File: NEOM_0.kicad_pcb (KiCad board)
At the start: 2 copper layers, 28 x 24 mm, 21 parts, among them U1 LM3940, U2 7_Pins_Header_PA0_PA6, U3 Reset Button, U4 STM32F070F6P6, U6 7_Pins_Header_PA7_PA14, U7 TPD4S012DRYR, U8 16Mhz, U9 USB_Micro_B

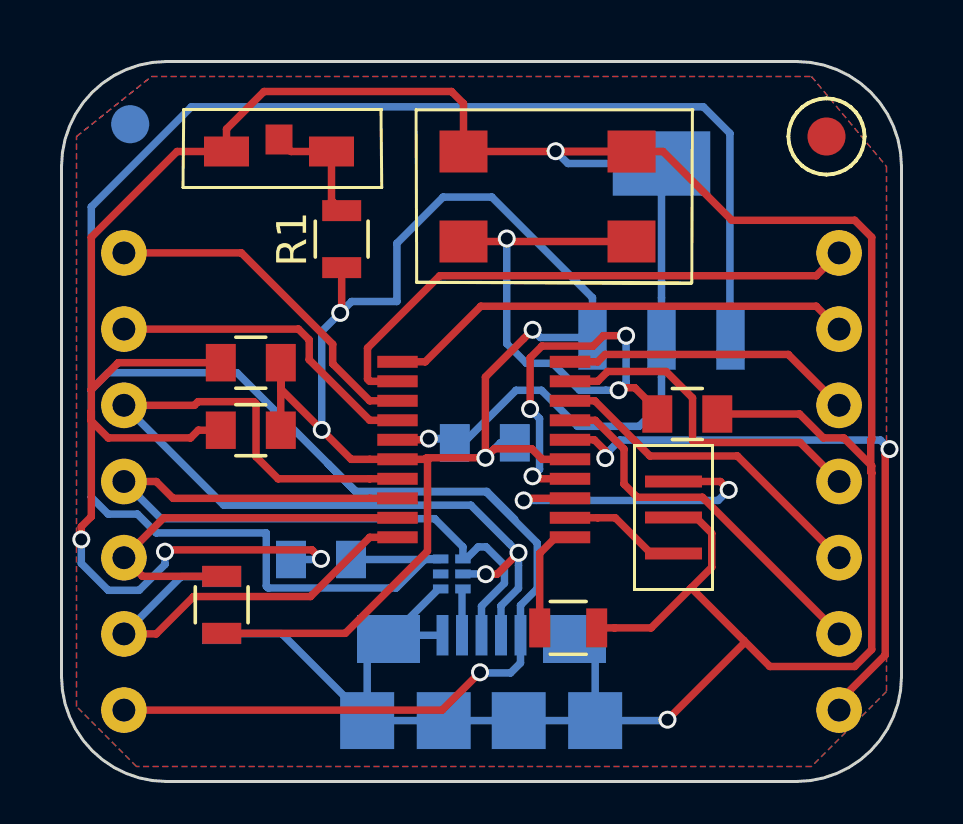
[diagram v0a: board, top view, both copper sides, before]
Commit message: Updated PCB with Footprint Fab..
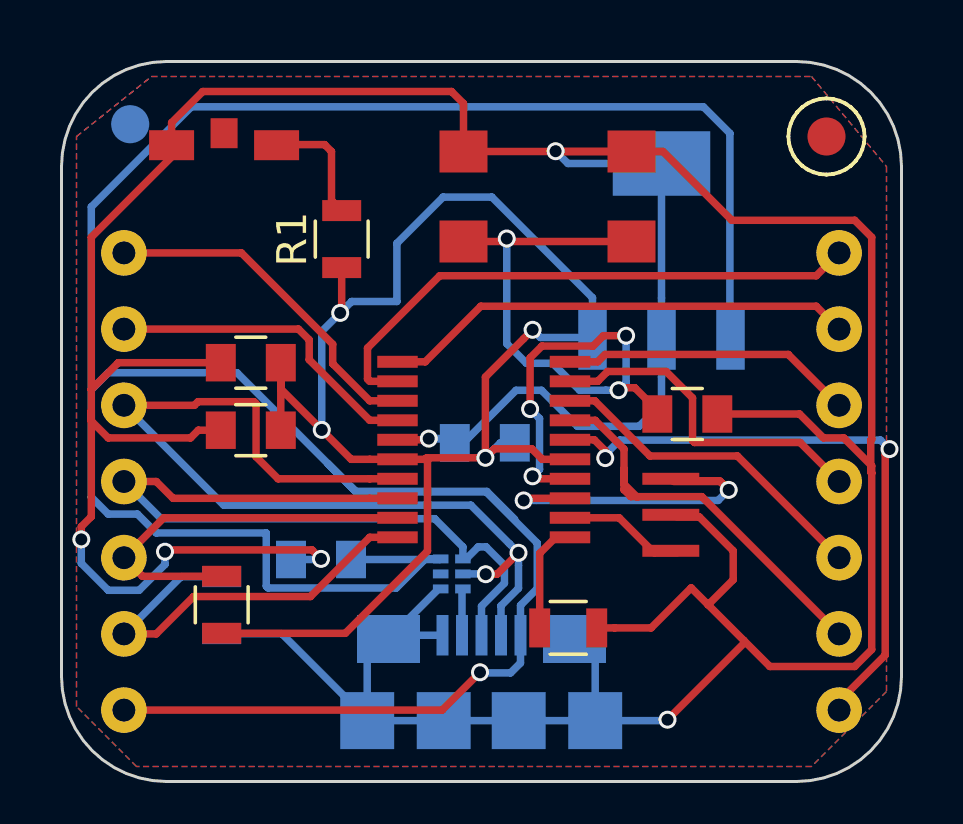
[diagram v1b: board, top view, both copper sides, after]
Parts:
- C1, C2, C3, C4, C5: footprint Capacitors_SMD:C_0805 -> Footprints2:C_0805
- D1: footprint Footprints:0805_LED -> Footprints2:0805_LED
- U1: footprint Footprints:LM3940 -> Footprints2:LM3940
- U3: footprint Footprints:Tactile_Button -> Footprints2:Tactile_Button
- U4: footprint Footprints:TSSOP20 -> Footprints2:TSSOP20
- U7: footprint Footprints:TPD4S012DRYR -> Footprints2:TPD4S012DRYR
- U8: footprint Footprints:16Mhz -> Footprints2:16Mhz
- moved D1 4.60 mm to (115.5, 92.1)
- moved U8 2.91 mm to (130.3, 104.1)
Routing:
- net Net-(U4-Pad3): track 10.5 -> 12.4 mm
- net Net-(U2-Pad2): track 12.6 -> 13.8 mm
- net GND: track 152.5 -> 153.5 mm

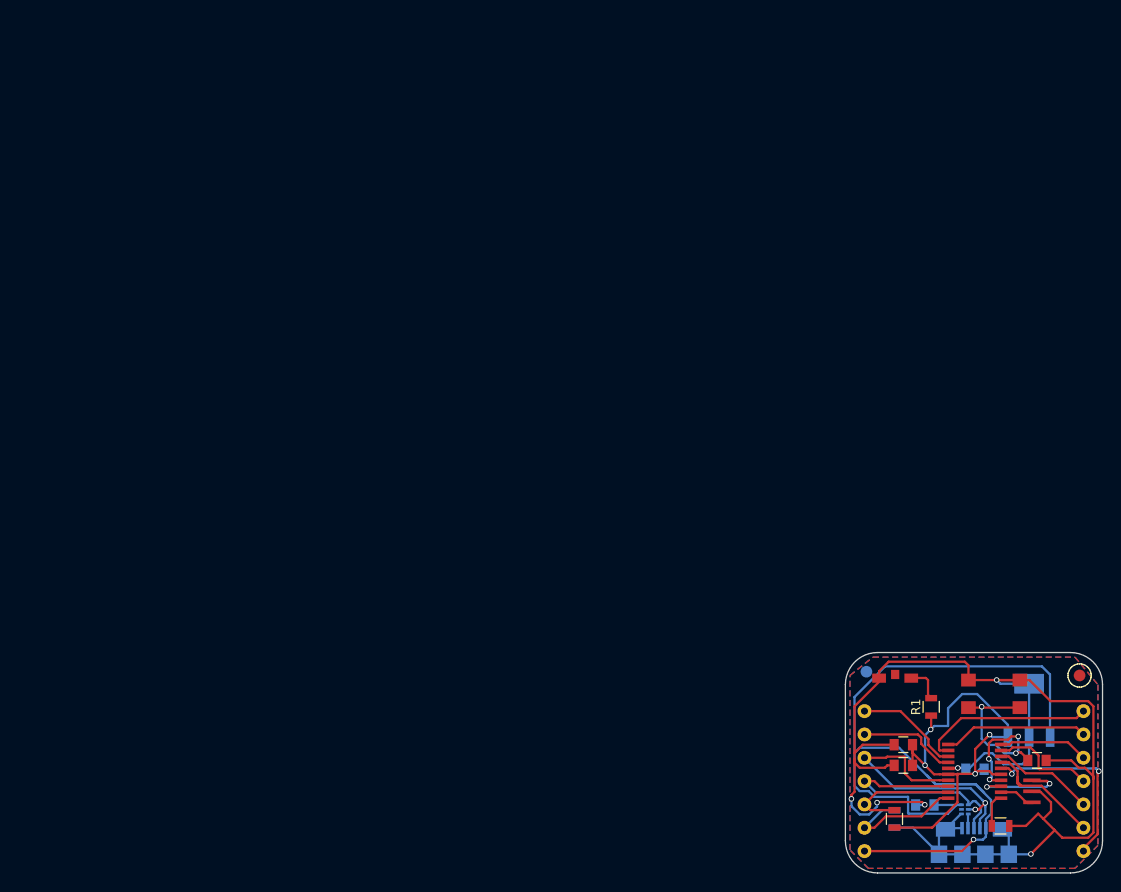
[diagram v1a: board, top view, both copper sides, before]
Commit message: Updated PCB: added defferintial pair routing to USB+/-...
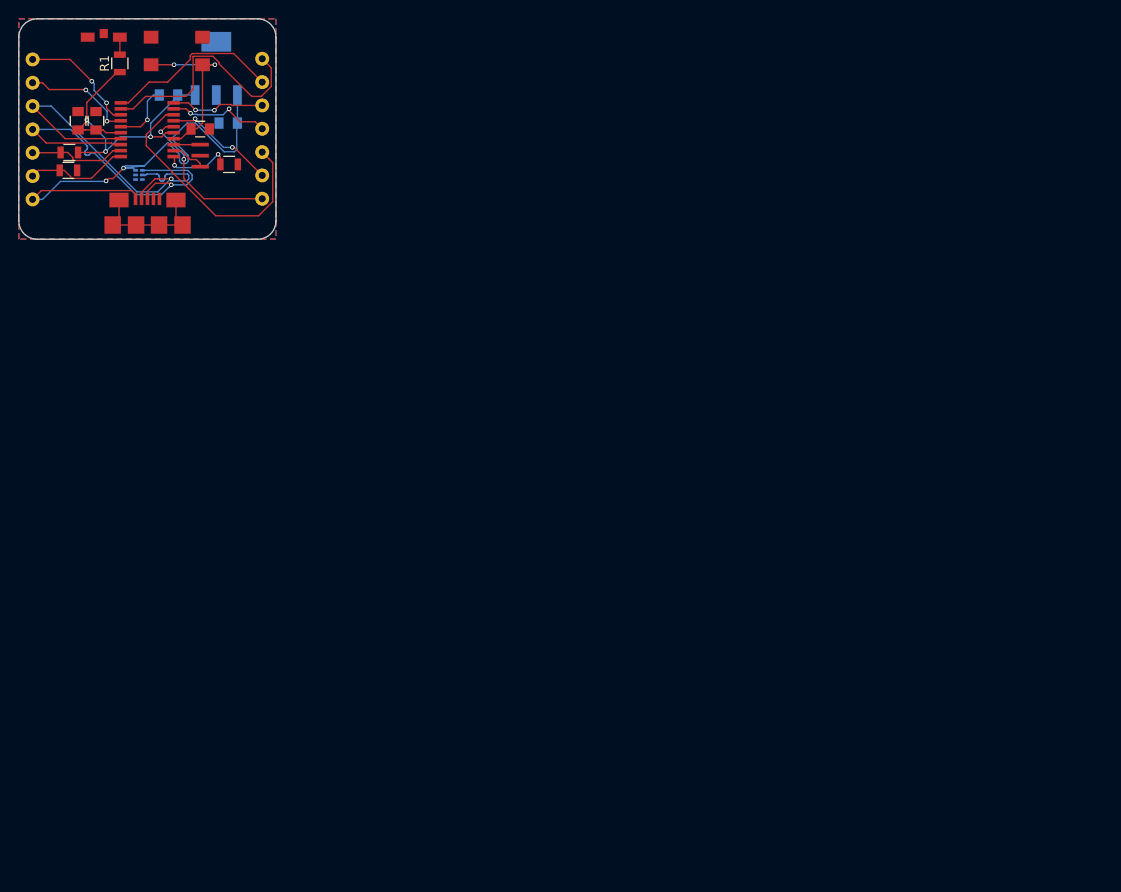
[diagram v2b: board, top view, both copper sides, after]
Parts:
- removed FID1, FID2: FIDUCIAL, Footprints2:MF_Aesthetics-FIDUCIAL_100MIL
- R3, U9: moved to F.Cu
- moved R2 115.5 mm to (25.5, 34.5), turned to 180 degrees
- moved U6 115.1 mm to (16.4, 32.0)
- moved C4 114.5 mm to (36.3, 28.3)
- moved R3 114.4 mm to (25.4, 36.5), turned to 0 degrees
- moved U2 114.2 mm to (51.6, 32.0)
- moved C5 114.1 mm to (39.8, 32.0)
- moved C2 114.0 mm to (26.4, 31.1), turned to 90 degrees
- moved U4 114.0 mm to (41.2, 38.5)
- moved U8 114.0 mm to (39.8, 34.9)
- moved U7 113.4 mm to (35.5, 37.0)
- moved U3 113.2 mm to (40.0, 28.0)
- moved U9 113.1 mm to (34.0, 42.5), turned to 0 degrees
- moved U1 112.8 mm to (41.5, 34.1)
- moved R1 112.8 mm to (31.0, 24.9)
- moved C1 111.1 mm to (28.4, 31.1), turned to 90 degrees
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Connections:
- net /USB_DM renamed /USB-
- net /USB_DP renamed /USB+
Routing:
- net GND: track 153.5 -> 20.4 mm, vias 6 -> 1
- net /VBUS: track 99.4 -> 55.3 mm, vias 1 -> 2
- net Net-(U2-Pad3): track 11.1 -> 28.6 mm
- net +3V3: track 52.9 -> 36.4 mm, vias 4 -> 3
- net /USB+: track 26.4 -> 42.4 mm, vias 0 -> 1
- net /USB-: track 31.6 -> 43.8 mm, vias 2 -> 1
- net Net-(U4-Pad3): track 12.4 -> 2.90 mm, vias 2 -> 0
- net /NRST: track 26.2 -> 18.5 mm, vias 5 -> 2
- net Net-(U2-Pad7): track 19.1 -> 26.6 mm
- net /BOOT0: track 3.72 -> 7.65 mm, vias 0 -> 2
- net Net-(U2-Pad1): track 20.9 -> 17.2 mm
- net Net-(U2-Pad6): track 15.8 -> 19.2 mm
- net /SWCLK: track 14.5 -> 11.2 mm
- net /SWDIO: track 13.2 -> 10.6 mm
- net Net-(D1-Pad2): track 3.90 -> 1.90 mm
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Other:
- outline, holes or cut-outs redrawn
- net class Default: clearance 0.2 -> 0.15; trace_width 0.25 -> 0.15; via_dia 0.6 -> 0.5; via_drill 0.4 -> 0.3
- rule trace_clearance: 0.2 -> 0.15
- rule trace_min: 0.2 -> 0.15
- rule via_min_size: 0.4 -> 0.5
